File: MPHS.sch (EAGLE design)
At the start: 22 parts, among them U1 SPI_FLASH-X25XXSMD, U2 MCP1701, U3 RFM69W

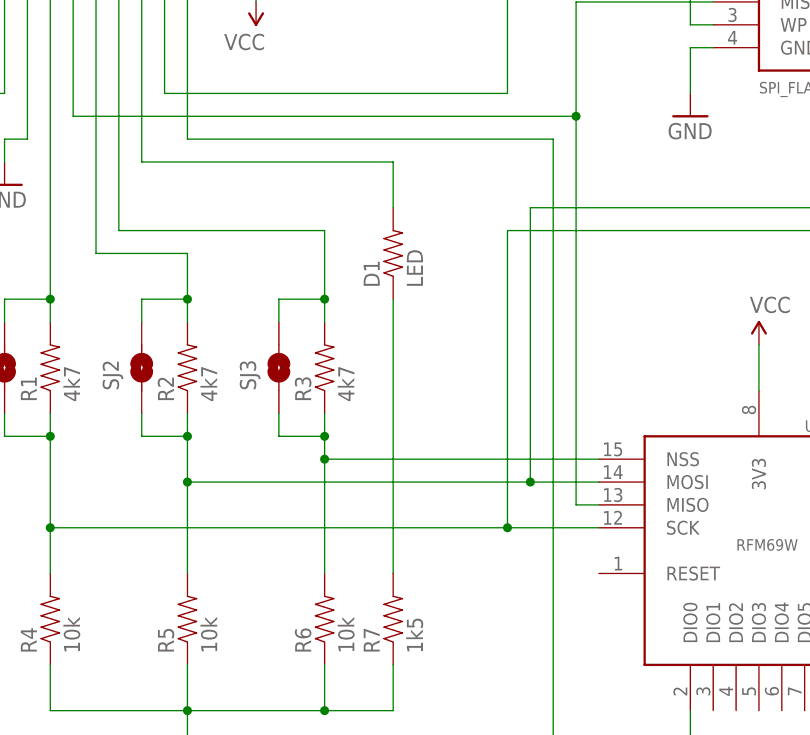
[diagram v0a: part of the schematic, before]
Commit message: New photo with LED installed (parts arrived)
Changed board layout and schematic to have proper LED component.  No
change to actual BOM or circuit.  Shot new photo of board with LED
installed.
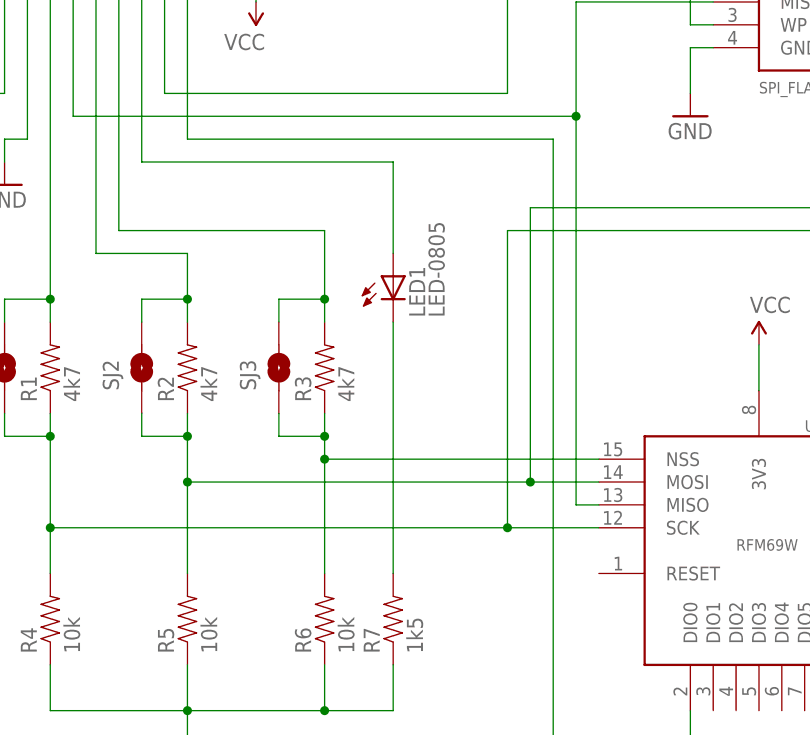
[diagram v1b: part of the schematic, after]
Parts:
- removed D1: LED, SparkFun-Resistors:RESISTOR0805-RES
- added LED1: LED-0805, ChipsParts:LED-0805
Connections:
- net N$13: now also LED1.A; no longer D1.2
- net N$15: now also LED1.C; no longer D1.1
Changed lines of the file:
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@@
 <part name="R7" library="SparkFun-Resistors" deviceset="RESISTOR" device="0805-RES" value="1k5"/>
 <part name="JP1" library="SparkFun-Connectors" deviceset="M10" device="&quot;"/>
-<part name="D1" library="SparkFun-Resistors" deviceset="RESISTOR" device="0805-RES" value="LED"/>
+<part name="LED1" library="ChipsParts" deviceset="LED" device="-0805"/>
 </parts>
 <sheets>
@@
 <attribute name="NAME" x="11.43" y="68.58" size="1.778" layer="95" rot="R270"/>
 </instance>
-<instance part="D1" gate="G$1" x="27.94" y="25.4" rot="R90"/>
+<instance part="LED1" gate="G$1" x="27.94" y="22.86"/>
 </instances>
 <busses>
@@
 <wire x1="0" y1="58.42" x2="0" y2="35.56" width="0.1524" layer="91"/>
 <wire x1="0" y1="35.56" x2="27.94" y2="35.56" width="0.1524" layer="91"/>
-<wire x1="27.94" y1="35.56" x2="27.94" y2="30.48" width="0.1524" layer="91"/>
+<wire x1="27.94" y1="35.56" x2="27.94" y2="25.4" width="0.1524" layer="91"/>
 <pinref part="JP1" gate="G$1" pin="7"/>
-<pinref part="D1" gate="G$1" pin="2"/>
+<pinref part="LED1" gate="G$1" pin="A"/>
 </segment>
 </net>
@@
 <segment>
 <pinref part="R7" gate="G$1" pin="2"/>
-<pinref part="D1" gate="G$1" pin="1"/>
-<wire x1="27.94" y1="20.32" x2="27.94" y2="-10.16" width="0.1524" layer="91"/>
-</segment>
-</net>
+<wire x1="27.94" y1="17.78" x2="27.94" y2="-10.16" width="0.1524" layer="91"/>
+<pinref part="LED1" gate="G$1" pin="C"/>
+</segment>
+</net>
